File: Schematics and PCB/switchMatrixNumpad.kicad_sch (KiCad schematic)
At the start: 116 parts, among them SW100 NUMPAD16, SW101 NUMPAD17, SW102 NUMPAD18, SW103 NUMPAD19, SW104 NUMPAD20, SW85 NUMPAD1, SW86 NUMPAD2, SW87 NUMPAD3, SW88 NUMPAD4, SW89 NUMPAD5, SW90 NUMPAD6, SW91 NUMPAD7, SW92 NUMPAD8, SW93 NUMPAD9, SW94 NUMPAD10, SW95 NUMPAD11, SW96 NUMPAD12, SW97 NUMPAD13, SW98 NUMPAD14, SW99 NUMPAD15

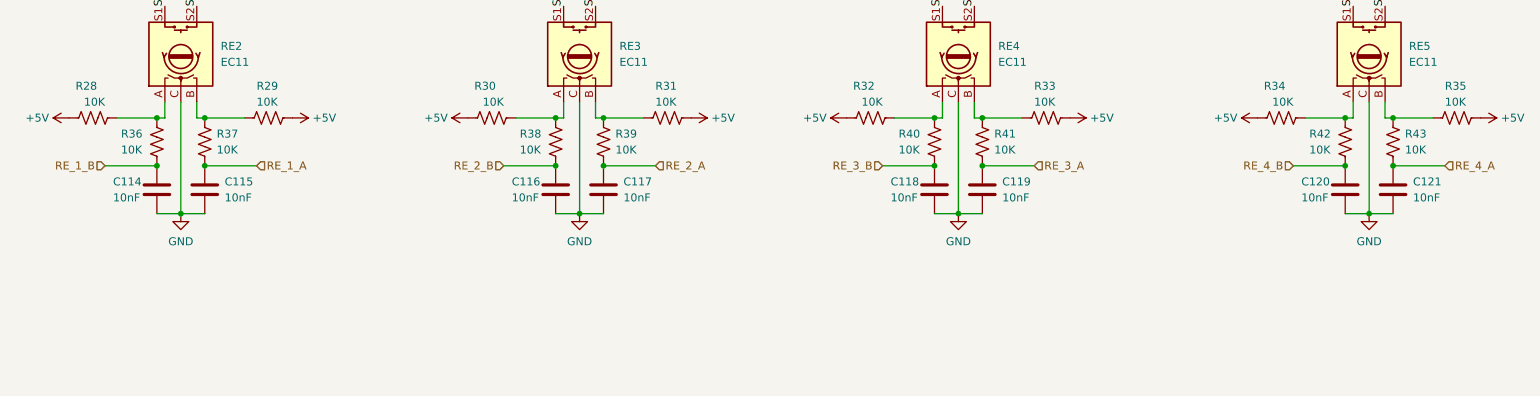
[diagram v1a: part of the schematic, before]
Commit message: Updated USB hub
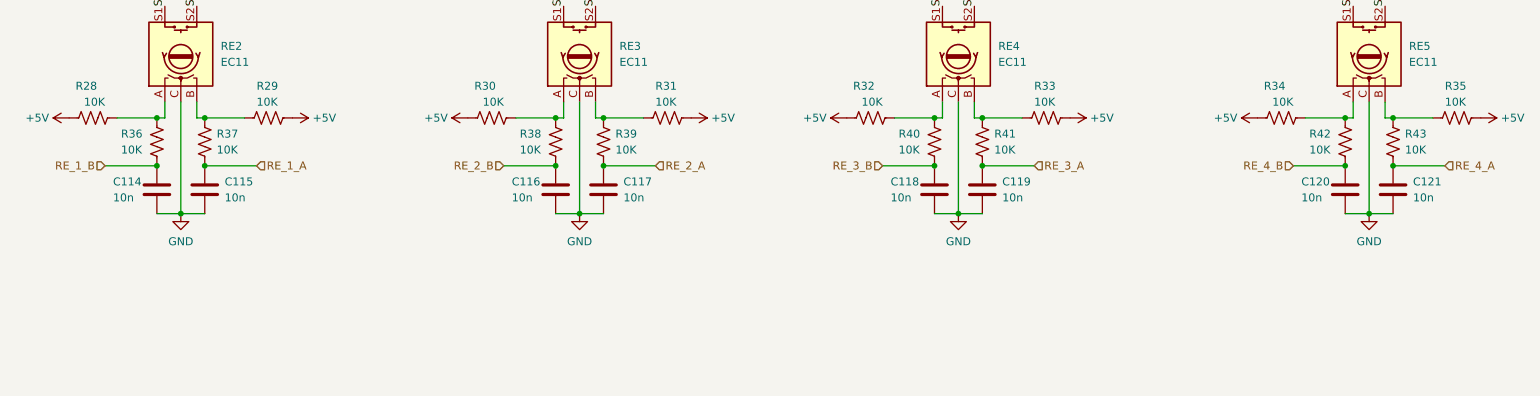
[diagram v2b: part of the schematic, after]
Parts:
- C114, C115, C116, C117, C118, C119, C120, C121: value 10nF -> 10n

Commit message: minor changes
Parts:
- removed C100, C101, C102, C103, C104, C105, C106, C107, C108, C109, C110, C111, C112, C113, C94, C95, C96, C97, C98, C99: 100n, Capacitor_SMD:C_0603_1608Metric, symbol Device:C
- removed C114, C115, C116, C117, C118, C119, C120, C121: 10n, Capacitor_SMD:C_0603_1608Metric, symbol Device:C
- removed R28, R29, R30, R31, R32, R33, R34, R35, R36, R37, R38, R39, R40, R41, R42, R43: 10K, Resistor_SMD:R_0603_1608Metric, symbol Device:R_US
- removed RGB100, RGB101, RGB102, RGB103, RGB104, RGB85, RGB86, RGB87, RGB88, RGB89, RGB90, RGB91, RGB92, RGB93, RGB94, RGB95, RGB96, RGB97, RGB98, RGB99: WS2812B, LED_SMD:LED_WS2812B_PLCC4_5.0x5.0mm_P3.2mm, symbol LED:WS2812B
- added C145, C149, C157, C161, C178, C190, C215, C219, C224, C225, C227, C228, C230, C231, C233, C234, C236, C239, C242, C245: 100n, Capacitor_SMD:C_0805_2012Metric, symbol Device:C
- added C153, C169, C199, C223, C226, C229, C232, C235, C237, C238, C240, C241: 100n, Capacitor_SMD:C_0603_1608Metric, symbol Device:C
- added R57, R58, R59, R60, R61, R62, R63, R64: 10K, Resistor_SMD:R_0603_1608Metric, symbol Device:R_US
- added RGB156, RGB160, RGB168, RGB172, RGB180, RGB184, RGB192, RGB196, RGB201, RGB202, RGB204, RGB205, RGB207, RGB208, RGB210, RGB211, RGB213, RGB216, RGB219, RGB222: WS2812B, LED_SMD:LED_WS2812B_PLCC4_5.0x5.0mm_P3.2mm, symbol LED:WS2812B
- renumbered D97 to D100, D98 to D101, D99 to D102, D100 to D103, D101 to D104, D102 to D105, D103 to D106, D104 to D107, D105 to D108, D106 to D109, D107 to D110, D108 to D111, D109 to D112, D110 to D113, D111 to D114, D112 to D115, D89 to D92, D90 to D93, D91 to D94, D92 to D95, D93 to D96, D94 to D97, D95 to D98, D96 to D99, R44 to R49, R45 to R50, R46 to R51, R47 to R52, SW99 to SW100, SW100 to SW101, SW101 to SW102, SW102 to SW103, SW103 to SW104, SW104 to SW105, SW85 to SW86, SW86 to SW87, SW87 to SW88, SW88 to SW89, SW89 to SW90, SW90 to SW91, SW91 to SW92, SW92 to SW93, SW93 to SW94, SW94 to SW95, SW95 to SW96, SW96 to SW97, SW97 to SW98, SW98 to SW99
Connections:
- net +5V: now also C145.1, C149.1, C157.1, C161.1, C178.1, C190.1, C215.1, C219.1, C224.1, C225.1, C227.1, C228.1, C230.1, C231.1, C233.1, C234.1, C236.1, C239.1, C242.1, C245.1, RGB156.1 (VDD), RGB160.1 (VDD), RGB168.1 (VDD), RGB172.1 (VDD), RGB180.1 (VDD), RGB184.1 (VDD), RGB192.1 (VDD), RGB196.1 (VDD), RGB201.1 (VDD), RGB202.1 (VDD), RGB204.1 (VDD), RGB205.1 (VDD), RGB207.1 (VDD), RGB208.1 (VDD), RGB210.1 (VDD), RGB211.1 (VDD), RGB213.1 (VDD), RGB216.1 (VDD), RGB219.1 (VDD), RGB222.1 (VDD); no longer R49.1, R50.1, R51.1, R52.1
- net GND: now also C145.2, C149.2, C153.2, C157.2, C161.2, C169.2, C178.2, C190.2, C199.2, C215.2, C219.2, C223.2, C224.2, C225.2, C226.2, C227.2, C228.2, C229.2, C230.2, C231.2, C232.2, C233.2, C234.2, C235.2, C236.2, C237.2, C238.2, C239.2, C240.2, C241.2, C242.2, C245.2, RGB156.3 (VSS), RGB160.3 (VSS), RGB168.3 (VSS), RGB172.3 (VSS), RGB180.3 (VSS), RGB184.3 (VSS), RGB192.3 (VSS), RGB196.3 (VSS), RGB201.3 (VSS), RGB202.3 (VSS), RGB204.3 (VSS), RGB205.3 (VSS), RGB207.3 (VSS), RGB208.3 (VSS), RGB210.3 (VSS), RGB211.3 (VSS), RGB213.3 (VSS), RGB216.3 (VSS), RGB219.3 (VSS), RGB222.3 (VSS)
- net RE_B_0: now reaches RE5.A
- net RE_B_0: now also C238.1, R63.1
- net RE_A_0: now reaches RE5.B
- net RE_A_0: now also C240.1, R64.1
- net RE_B_1: now reaches RE2.A
- net RE_B_1: now also C153.1, R57.1
- net RE_B_2: now reaches RE3.A
- net RE_B_2: now also C223.1, R59.1
- net RE_A_2: now reaches RE3.B
- net RE_A_2: now also C226.1, R60.1
- net RE_B_3: now reaches RE4.A
- net RE_B_3: now also C232.1, R61.1
- net RE_A_1: now reaches RE2.B
- net RE_A_1: now also C169.1, R58.1
- net RE_A_3: now reaches RE4.B
- net RE_A_3: now also C235.1, R62.1
- net COL_0_N renamed COL0
- net COL0: now also RE4.S2, C237.1; no longer RE2.S1
- net COL_1_N renamed COL1
- net COL1: now also RE3.S2, C229.1; no longer RE3.S1
- net COL_2_N renamed COL2
- net COL2: now also RE2.S2, C199.1; no longer RE4.S1
- net COL_3_N renamed COL3
- net COL3: now also RE5.S2, C241.1; no longer RE5.S1
- net ROW_0_N renamed ROW0
- net ROW_1_N renamed ROW1
- net ROW_2_N renamed ROW2
- net ROW_3_N renamed ROW3
- net ROW_4_N renamed ROW4
- net ROW_5_N renamed ROW5
- net SW1.2: no longer names the net of D92.2 (A)
- net SW1.2: now also RE4.S1; no longer RE2.S2
- net SW2.2: no longer names the net of D93.2 (A)
- net SW2.2: now also RE3.S1; no longer RE3.S2
- net SW3.2: no longer names the net of D94.2 (A)
- net SW3.2: now also RE2.S1; no longer RE4.S2
- net SW4.2: no longer names the net of D95.2 (A)
- net SW4.2: now also RE5.S1; no longer RE5.S2
- new net: RGB213.2 (DOUT), RGB216.4 (DIN)
- new net: RGB210.2 (DOUT), RGB213.4 (DIN)
- new net: RGB184.2 (DOUT), RGB196.4 (DIN)
- new net: RGB172.2 (DOUT), RGB184.4 (DIN)
- new net: RGB204.2 (DOUT), RGB207.4 (DIN)
- new net: RGB201.2 (DOUT), RGB204.4 (DIN)
- new net: RGB208.2 (DOUT), RGB211.4 (DIN)
- new net: RGB205.2 (DOUT), RGB208.4 (DIN)
- new net: RGB219.2 (DOUT), RGB222.4 (DIN)
- new net: RGB216.2 (DOUT), RGB219.4 (DIN)
- new net: RGB180.2 (DOUT), RGB192.4 (DIN)
- new net: RGB168.2 (DOUT), RGB180.4 (DIN)
- new net: RGB156.2 (DOUT), RGB168.4 (DIN)
- new net: RGB207.2 (DOUT), RGB210.4 (DIN)
- new net: RGB192.2 (DOUT), RGB201.4 (DIN)
- new net: RGB160.4 (DIN), RGB222.2 (DOUT)
- new net: RGB196.2 (DOUT), RGB202.4 (DIN)
- new net: RGB202.2 (DOUT), RGB205.4 (DIN)
- new net: RGB160.2 (DOUT), RGB172.4 (DIN)
- new net +3V3: R49.1, R50.1, R51.1, R52.1, R57.2, R58.2, R59.2, R60.2, R61.2, R62.2, R63.2, R64.2
- new net RGB_IN: RGB156.4 (DIN)
- new net RGB_OUT: RGB211.2 (DOUT)
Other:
- note added: "LED matrix"
- note added: "Rotary encoders"
- note added: "Switch matrix"
- moved on the sheet: D100, D101, D102, D103, D104, D105, D106, D107, D108, D109, D110, D111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

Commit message: layout improvements
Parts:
- C100: renamed from C227; footprint Capacitor_SMD:C_0805_2012Metric -> Capacitor_SMD:C_0603_1608Metric
- C101: renamed from C230; footprint Capacitor_SMD:C_0805_2012Metric -> Capacitor_SMD:C_0603_1608Metric
- C102: renamed from C233; footprint Capacitor_SMD:C_0805_2012Metric -> Capacitor_SMD:C_0603_1608Metric
- C103: renamed from C236; footprint Capacitor_SMD:C_0805_2012Metric -> Capacitor_SMD:C_0603_1608Metric
- C104: renamed from C239; footprint Capacitor_SMD:C_0805_2012Metric -> Capacitor_SMD:C_0603_1608Metric
- C105: renamed from C242; footprint Capacitor_SMD:C_0805_2012Metric -> Capacitor_SMD:C_0603_1608Metric
- C106: renamed from C245; footprint Capacitor_SMD:C_0805_2012Metric -> Capacitor_SMD:C_0603_1608Metric
- C107: renamed from C149; footprint Capacitor_SMD:C_0805_2012Metric -> Capacitor_SMD:C_0603_1608Metric
- C108: renamed from C161; footprint Capacitor_SMD:C_0805_2012Metric -> Capacitor_SMD:C_0603_1608Metric
- C109: renamed from C190; footprint Capacitor_SMD:C_0805_2012Metric -> Capacitor_SMD:C_0603_1608Metric
- C110: renamed from C219; footprint Capacitor_SMD:C_0805_2012Metric -> Capacitor_SMD:C_0603_1608Metric
- C111: renamed from C225; footprint Capacitor_SMD:C_0805_2012Metric -> Capacitor_SMD:C_0603_1608Metric
- C112: renamed from C228; footprint Capacitor_SMD:C_0805_2012Metric -> Capacitor_SMD:C_0603_1608Metric
- C113: renamed from C231; footprint Capacitor_SMD:C_0805_2012Metric -> Capacitor_SMD:C_0603_1608Metric
- C114: renamed from C234; footprint Capacitor_SMD:C_0805_2012Metric -> Capacitor_SMD:C_0603_1608Metric
- C95: renamed from C145; footprint Capacitor_SMD:C_0805_2012Metric -> Capacitor_SMD:C_0603_1608Metric
- C96: renamed from C157; footprint Capacitor_SMD:C_0805_2012Metric -> Capacitor_SMD:C_0603_1608Metric
- C97: renamed from C178; footprint Capacitor_SMD:C_0805_2012Metric -> Capacitor_SMD:C_0603_1608Metric
- C98: renamed from C215; footprint Capacitor_SMD:C_0805_2012Metric -> Capacitor_SMD:C_0603_1608Metric
- C99: renamed from C224; footprint Capacitor_SMD:C_0805_2012Metric -> Capacitor_SMD:C_0603_1608Metric
- RGB100: renamed from RGB196; footprint LED_SMD:LED_WS2812B_PLCC4_5.0x5.0mm_P3.2mm -> mechpad:6028_LED
- RGB101: renamed from RGB202; footprint LED_SMD:LED_WS2812B_PLCC4_5.0x5.0mm_P3.2mm -> mechpad:6028_LED
- RGB102: renamed from RGB205; footprint LED_SMD:LED_WS2812B_PLCC4_5.0x5.0mm_P3.2mm -> mechpad:6028_LED
- RGB103: renamed from RGB208; footprint LED_SMD:LED_WS2812B_PLCC4_5.0x5.0mm_P3.2mm -> mechpad:6028_LED
- RGB104: renamed from RGB211; footprint LED_SMD:LED_WS2812B_PLCC4_5.0x5.0mm_P3.2mm -> mechpad:6028_LED
- RGB85: renamed from RGB156; footprint LED_SMD:LED_WS2812B_PLCC4_5.0x5.0mm_P3.2mm -> mechpad:6028_LED
- RGB86: renamed from RGB168; footprint LED_SMD:LED_WS2812B_PLCC4_5.0x5.0mm_P3.2mm -> mechpad:6028_LED
- RGB87: renamed from RGB180; footprint LED_SMD:LED_WS2812B_PLCC4_5.0x5.0mm_P3.2mm -> mechpad:6028_LED
- RGB88: renamed from RGB192; footprint LED_SMD:LED_WS2812B_PLCC4_5.0x5.0mm_P3.2mm -> mechpad:6028_LED
- RGB89: renamed from RGB201; footprint LED_SMD:LED_WS2812B_PLCC4_5.0x5.0mm_P3.2mm -> mechpad:6028_LED
- RGB90: renamed from RGB204; footprint LED_SMD:LED_WS2812B_PLCC4_5.0x5.0mm_P3.2mm -> mechpad:6028_LED
- RGB91: renamed from RGB207; footprint LED_SMD:LED_WS2812B_PLCC4_5.0x5.0mm_P3.2mm -> mechpad:6028_LED
- RGB92: renamed from RGB210; footprint LED_SMD:LED_WS2812B_PLCC4_5.0x5.0mm_P3.2mm -> mechpad:6028_LED
- RGB93: renamed from RGB213; footprint LED_SMD:LED_WS2812B_PLCC4_5.0x5.0mm_P3.2mm -> mechpad:6028_LED
- RGB94: renamed from RGB216; footprint LED_SMD:LED_WS2812B_PLCC4_5.0x5.0mm_P3.2mm -> mechpad:6028_LED
- RGB95: renamed from RGB219; footprint LED_SMD:LED_WS2812B_PLCC4_5.0x5.0mm_P3.2mm -> mechpad:6028_LED
- RGB96: renamed from RGB222; footprint LED_SMD:LED_WS2812B_PLCC4_5.0x5.0mm_P3.2mm -> mechpad:6028_LED
- RGB97: renamed from RGB160; footprint LED_SMD:LED_WS2812B_PLCC4_5.0x5.0mm_P3.2mm -> mechpad:6028_LED
- RGB98: renamed from RGB172; footprint LED_SMD:LED_WS2812B_PLCC4_5.0x5.0mm_P3.2mm -> mechpad:6028_LED
- RGB99: renamed from RGB184; footprint LED_SMD:LED_WS2812B_PLCC4_5.0x5.0mm_P3.2mm -> mechpad:6028_LED
- renumbered C241 to C115, C199 to C116, C229 to C117, C237 to C118, C238 to C119, C240 to C120, C153 to C121, C169 to C122, C223 to C123, C226 to C124, C232 to C125, C235 to C126, D103 to D100, D104 to D101, D105 to D102, D106 to D103, D107 to D104, D108 to D105, D109 to D106, D110 to D107, D111 to D108, D112 to D109, D113 to D110, D114 to D111, D115 to D112, D92 to D89, D93 to D90, D94 to D91, D95 to D92, D96 to D93, D97 to D94, D98 to D95, D99 to D96, D100 to D97, D101 to D98, D102 to D99, R49 to R30, R50 to R31, R51 to R32, R52 to R33, R63 to R34, R64 to R35, R57 to R36, R58 to R37, R59 to R38, R60 to R39, R61 to R40, R62 to R41, RE5 to RE2, RE2 to RE3, RE3 to RE4, RE4 to RE5, SW101 to SW100, SW102 to SW101, SW103 to SW102, SW104 to SW103, SW105 to SW104, SW86 to SW85, SW87 to SW86, SW88 to SW87, SW89 to SW88, SW90 to SW89, SW91 to SW90, SW92 to SW91, SW93 to SW92, SW94 to SW93, SW95 to SW94, SW96 to SW95, SW97 to SW96, SW98 to SW97, SW99 to SW98, SW100 to SW99
